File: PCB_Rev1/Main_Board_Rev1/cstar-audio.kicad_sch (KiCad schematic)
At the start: 0 parts

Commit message: LDO component files imported
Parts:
- added J?? (x2): 532610771, CSTAR-MainBoard-Footprints:MOLEX_532610771, symbol 532610771:532610771
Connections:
- new net +3V3: J??.3, J??.3
- new net GND: J??.2, J??.2, J??.S1 (SHIELD1), J??.S1 (SHIELD1), J??.S2 (SHIELD2), J??.S2 (SHIELD2)
- no-connect marks 0 -> 2
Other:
- note added: "Mic Board 1 (Unidirectional - Delamination)"
- note added: "Mic Board 2 (Directional - Environment)"

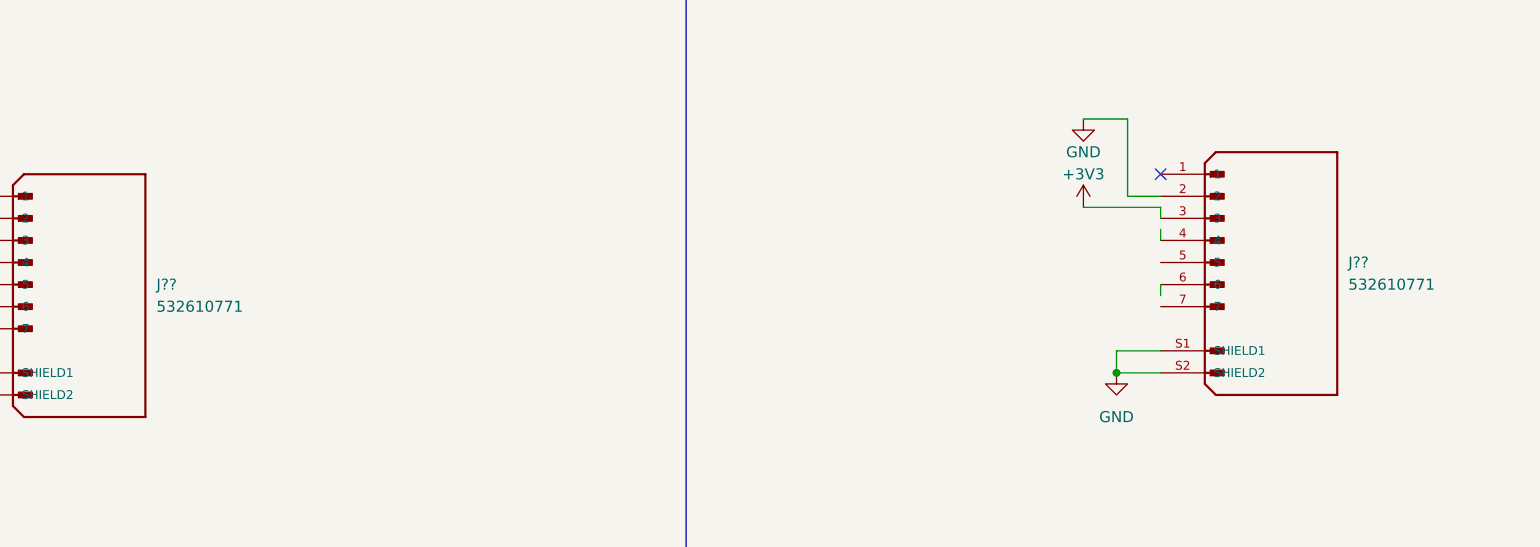
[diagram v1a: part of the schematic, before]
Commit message: LDO footprint assigned
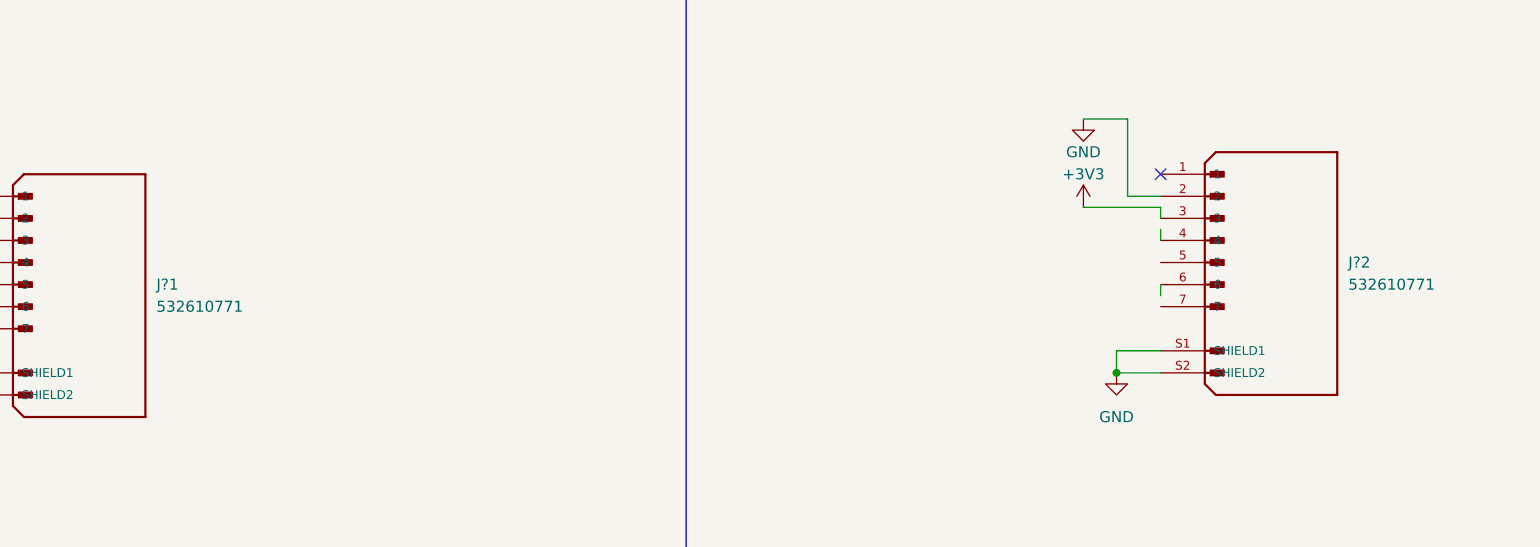
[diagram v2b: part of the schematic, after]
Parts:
- gave numbers to parts that had none: 2
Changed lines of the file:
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@@
 		(dnp no)
 		(fields_autoplaced yes)
-		(property "Reference" "J??"
+		(property "Reference" "J?1"
 			(at 91.44 100.3299 0)
 			(effects
@@
 			(project "Main_Board_Rev1"
 				(path "/8f5a23de-a1fa-4202-92fb-c2ac3de0338c/985328a3-4662-4f3a-8cff-b03fc4b452cf"
-					(reference "J??")
+					(reference "J?1")
 					(unit 1)
 				)
@@
 		(dnp no)
 		(fields_autoplaced yes)
-		(property "Reference" "J??"
+		(property "Reference" "J?2"
 			(at 228.6 97.7899 0)
 			(effects
@@
 			(project "Main_Board_Rev1"
 				(path "/8f5a23de-a1fa-4202-92fb-c2ac3de0338c/985328a3-4662-4f3a-8cff-b03fc4b452cf"
-					(reference "J??")
+					(reference "J?2")
 					(unit 1)
 				)
